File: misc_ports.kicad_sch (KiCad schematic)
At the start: 31 parts

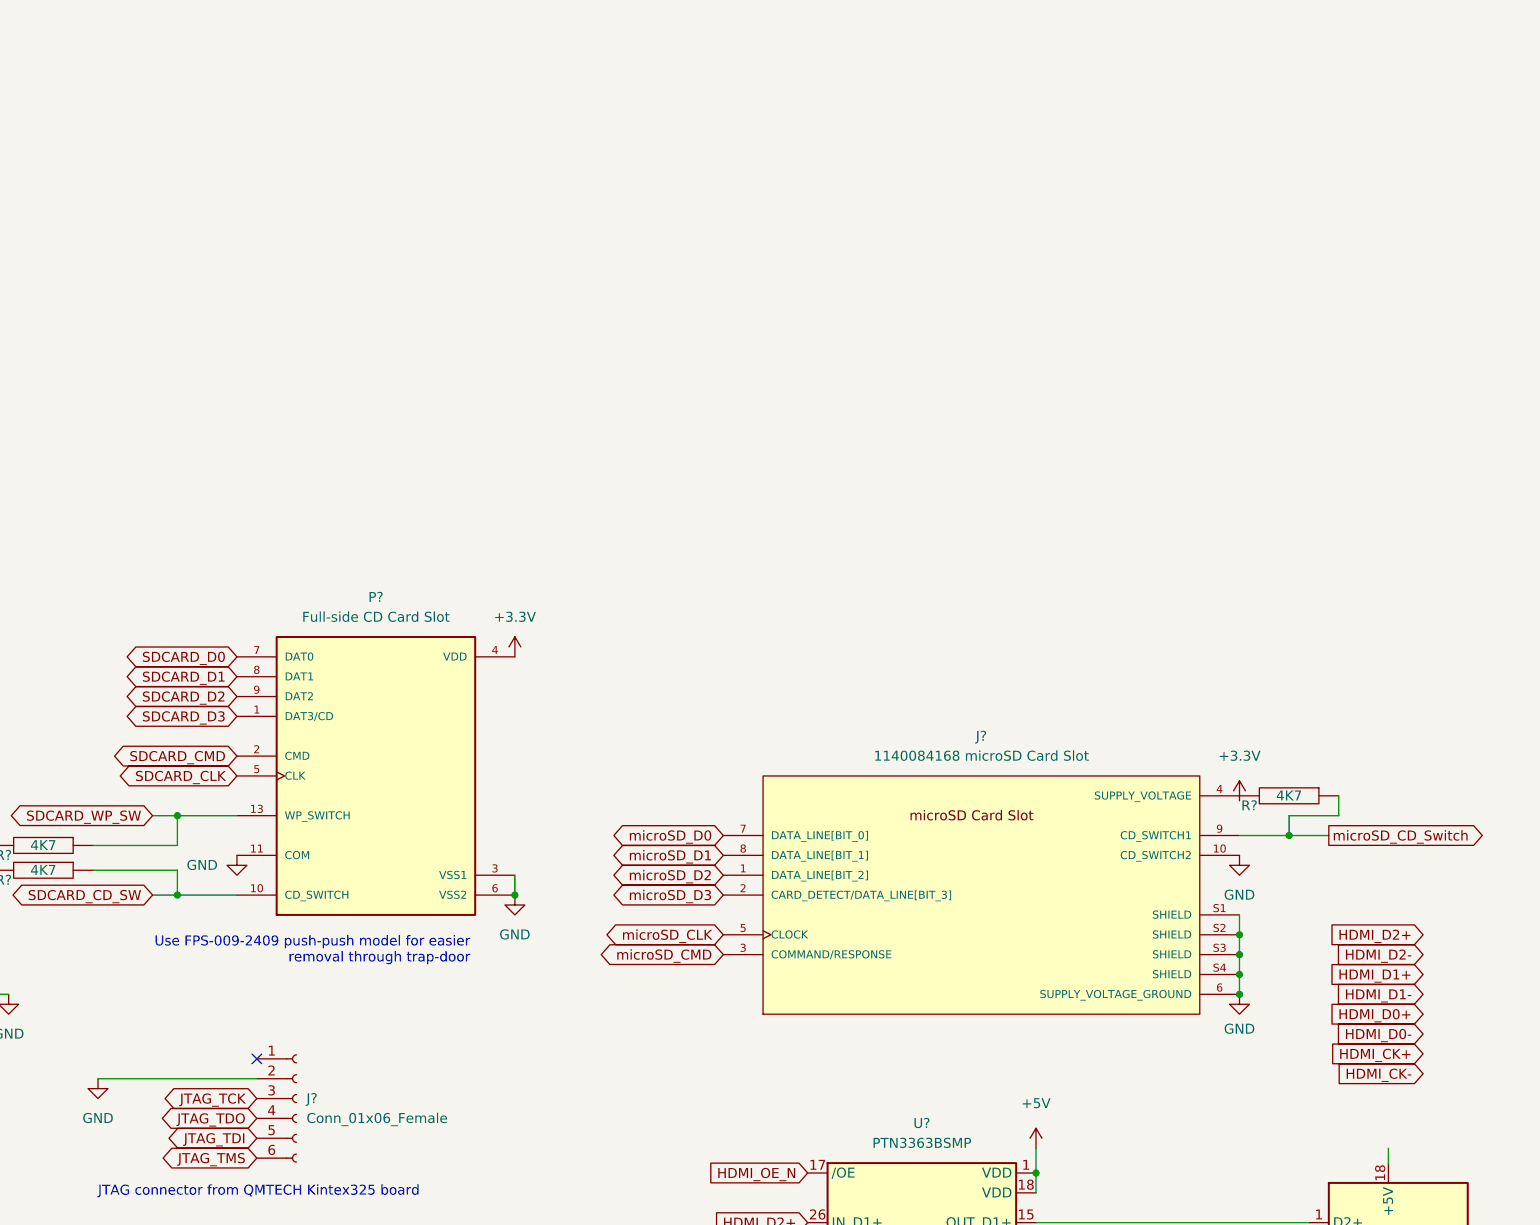
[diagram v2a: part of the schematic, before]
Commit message: plumb all direct FPGA signals.
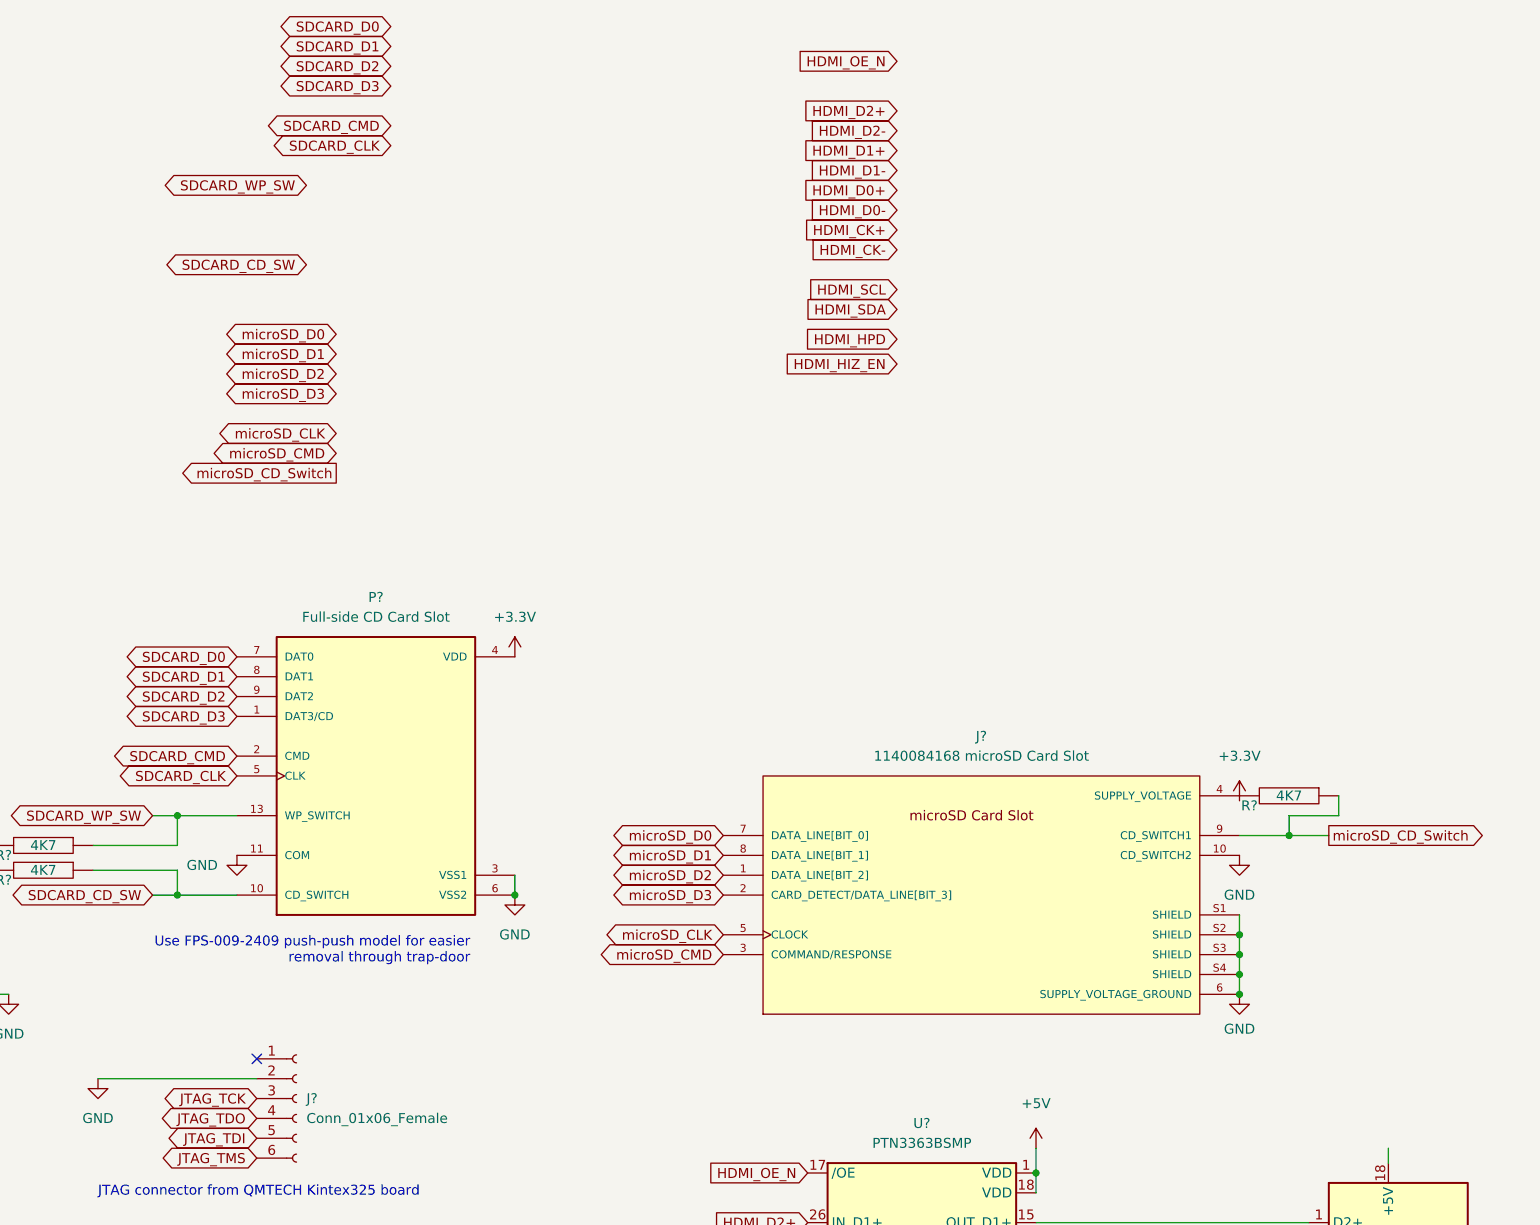
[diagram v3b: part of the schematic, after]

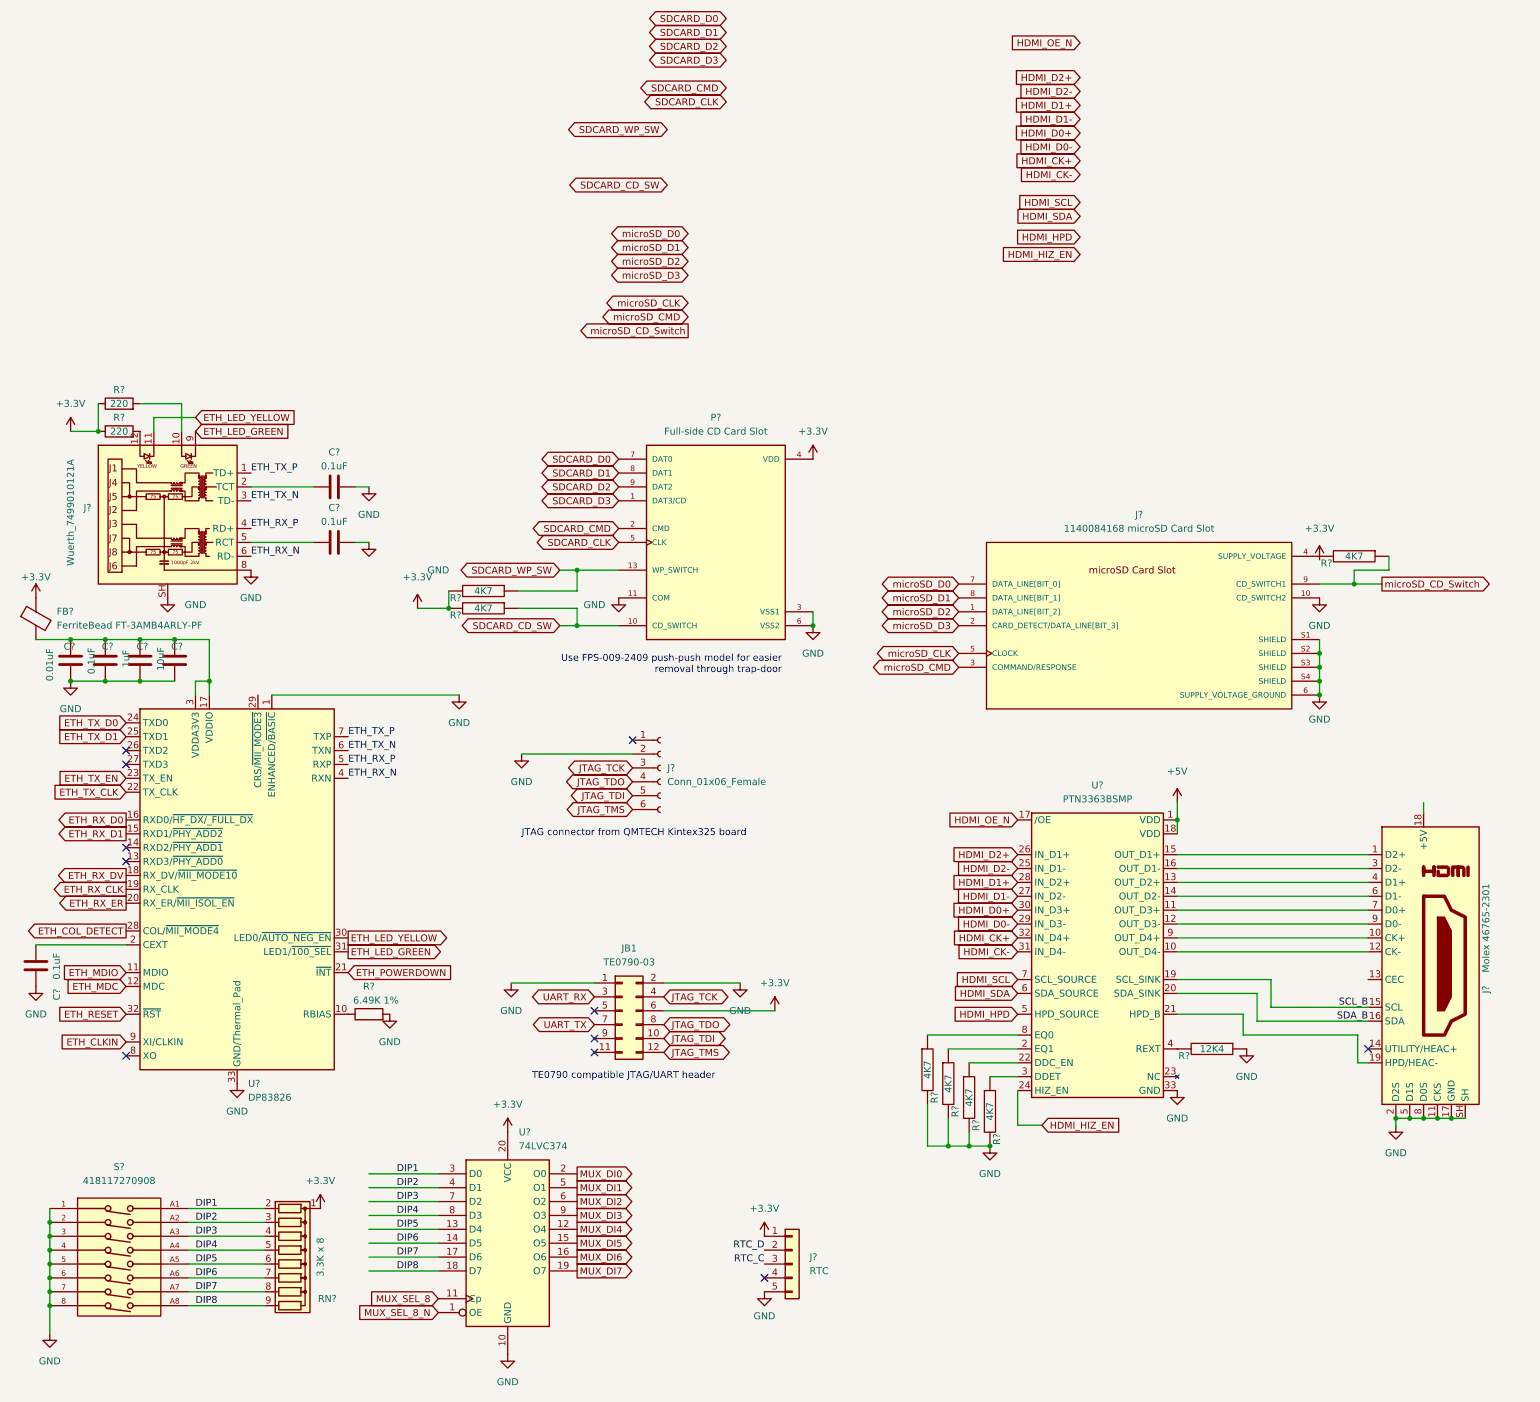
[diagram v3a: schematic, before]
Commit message: beautify the schematics, especially the title-page
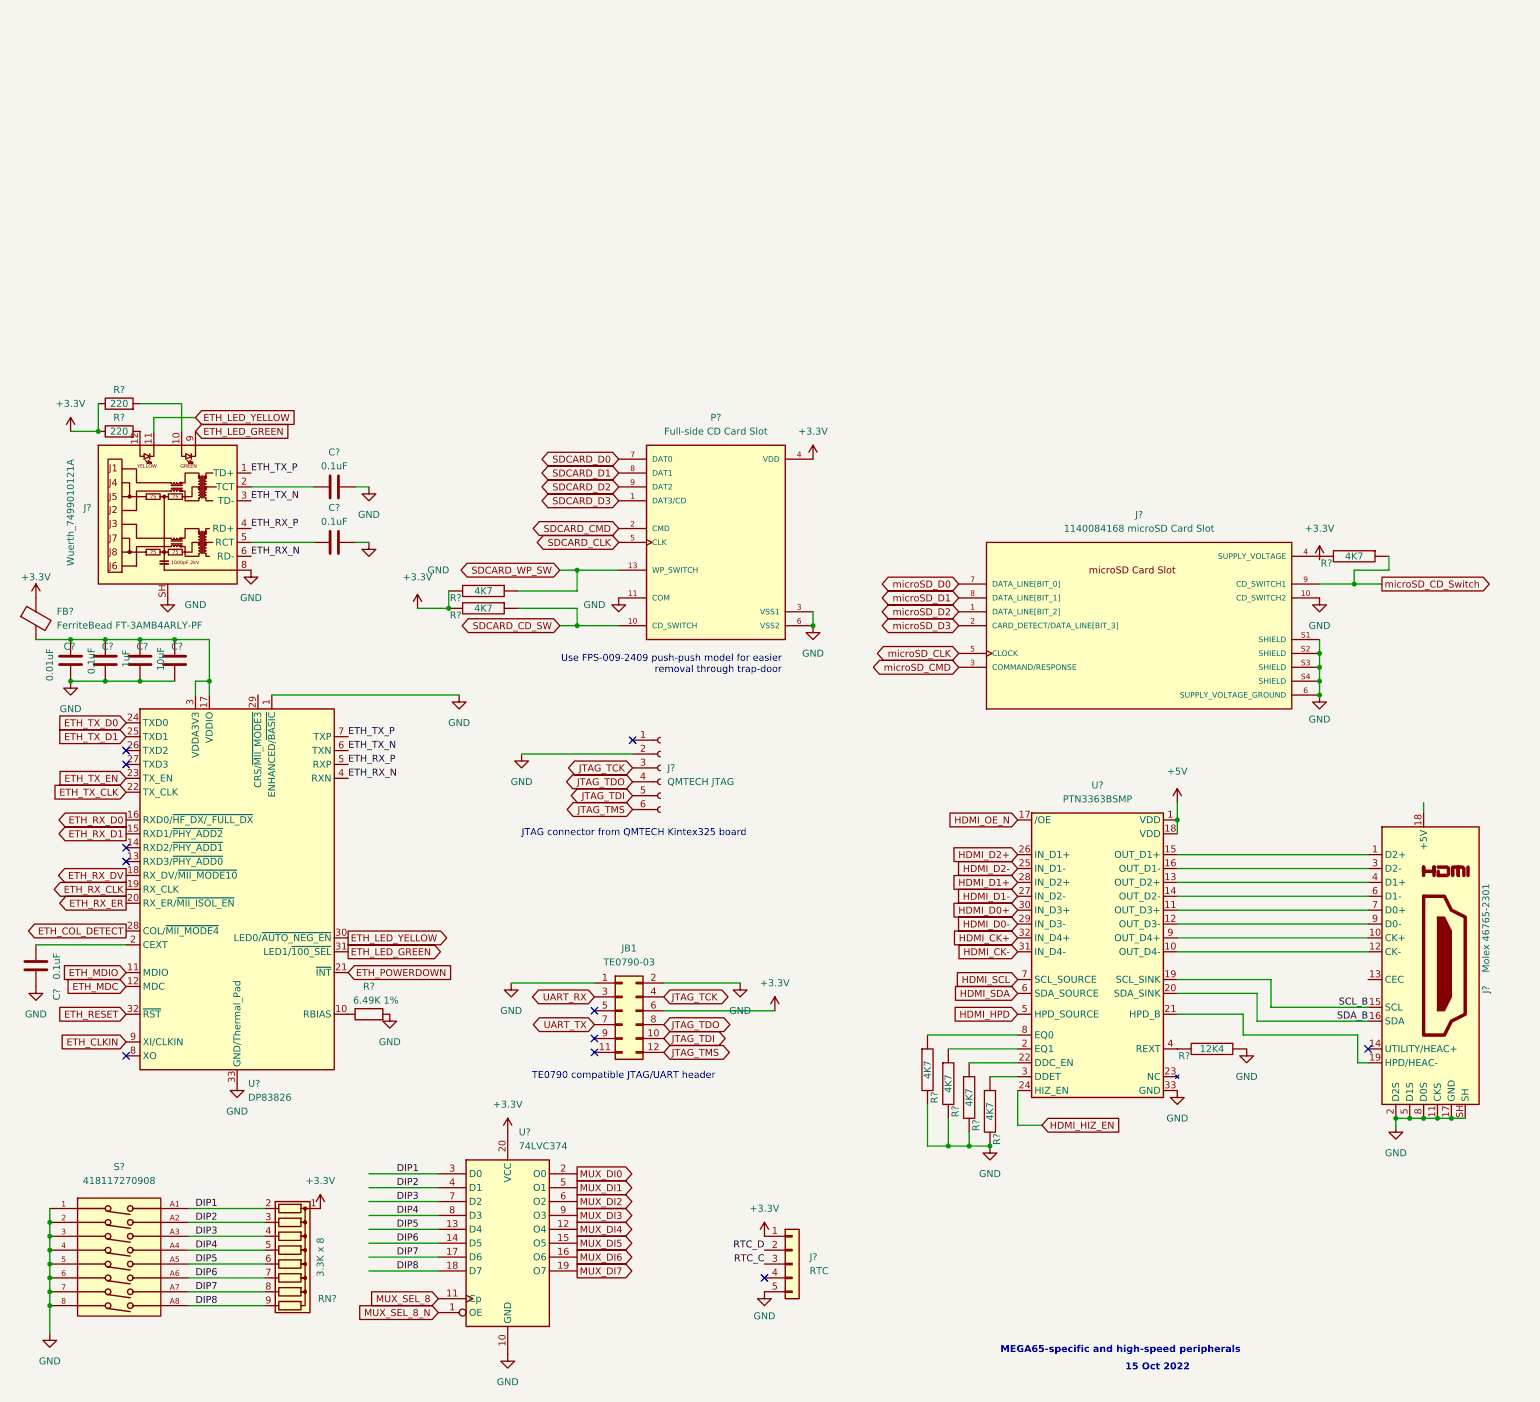
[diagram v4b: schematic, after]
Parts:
- J?: value Conn_01x06_Female -> QMTECH JTAG
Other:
- note added: "15 Oct 2022"
- note added: "MEGA65-specific and high-speed peripherals"

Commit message: add all missing footprints
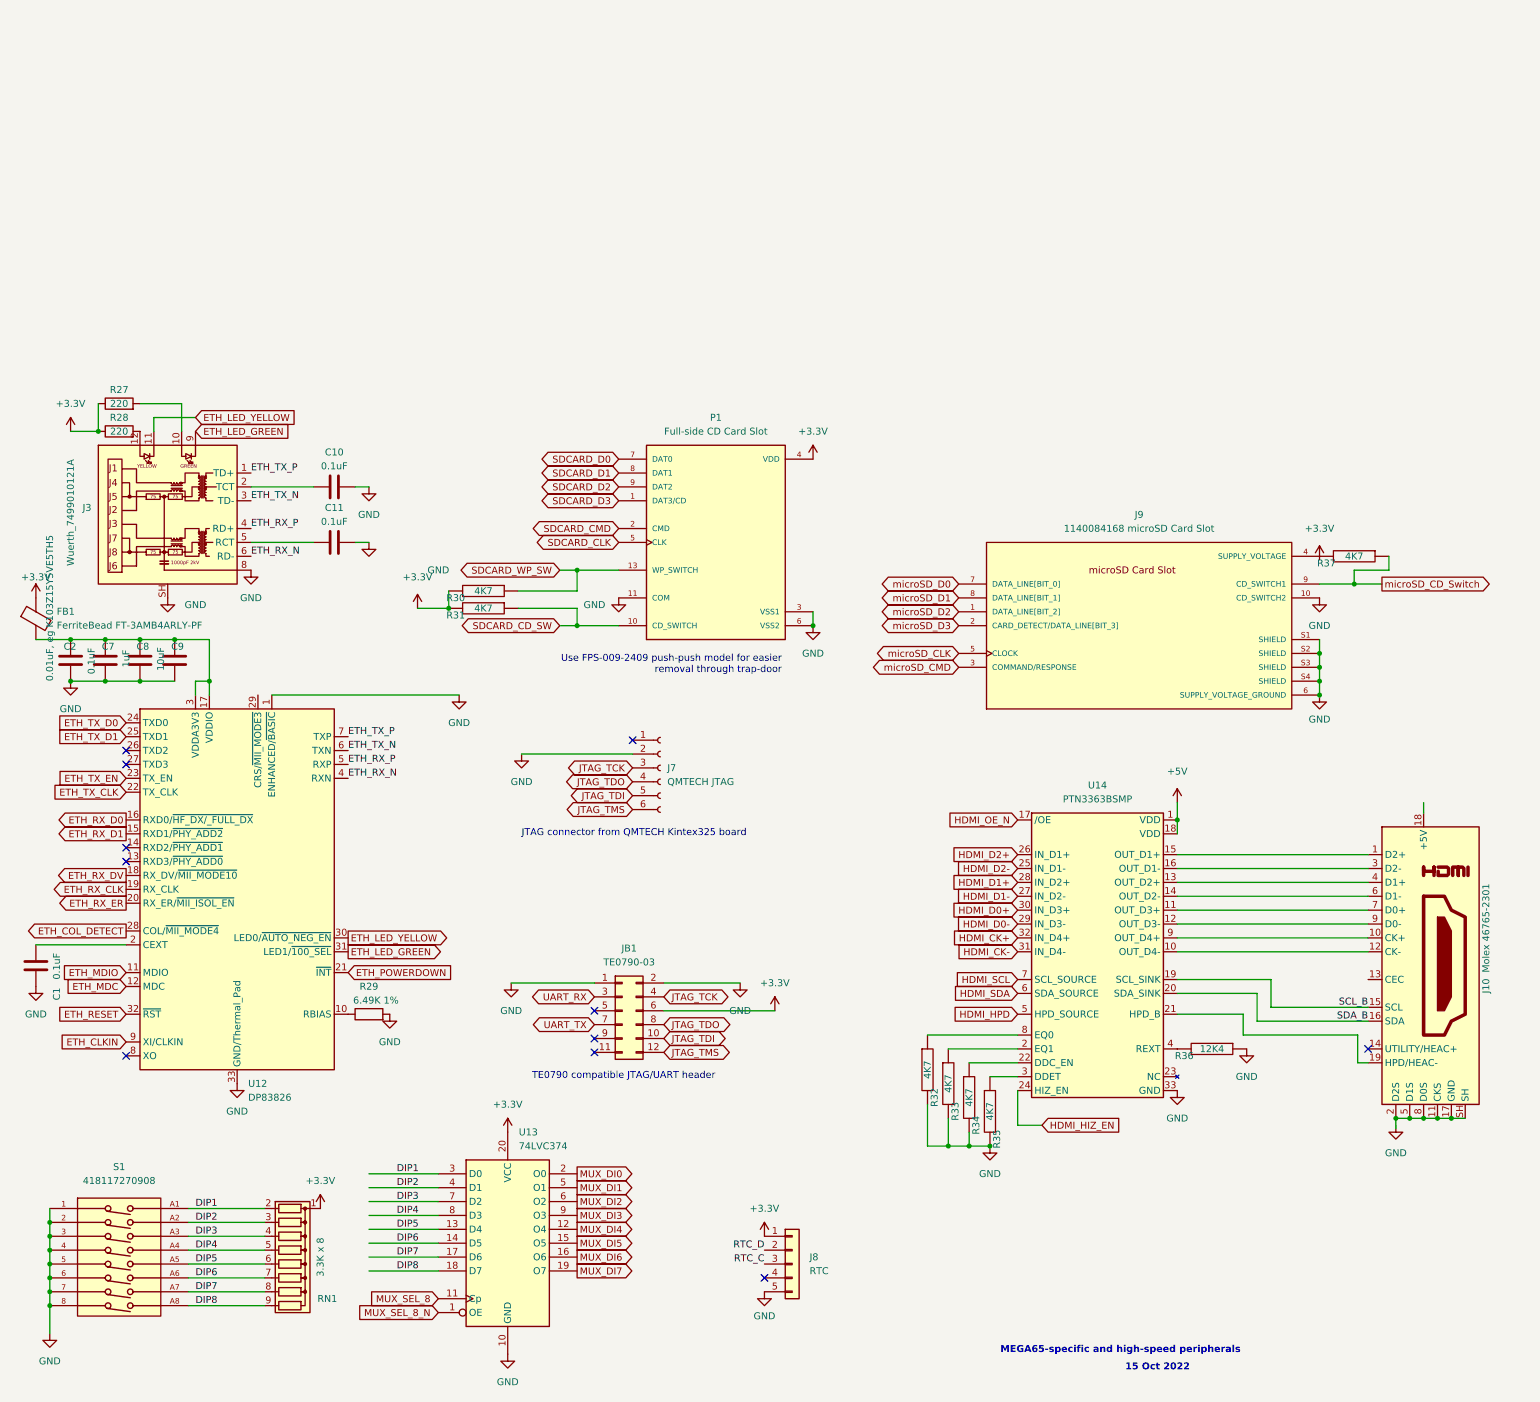
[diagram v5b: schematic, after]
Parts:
- C1, C10, C11, C7, C8, C9: renamed from C?; footprint (none) -> Capacitor_THT:C_Disc_D6.0mm_W4.4mm_P5.00mm
- C2: renamed from C?; value 0.01uF -> 0.01uF, eg K103Z15Y5VE5TH5; footprint (none) -> Capacitor_THT:C_Disc_D6.0mm_W4.4mm_P5.00mm
- gave numbers to parts that had none: 23
